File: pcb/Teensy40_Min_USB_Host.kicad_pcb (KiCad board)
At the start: 2 copper layers, 17.8 x 45.7 mm, 17 parts, among them J1 USB_A, J2 Conn_01x14, J3 Conn_01x14, U1 TPD3S014, U2 Teensy4.0

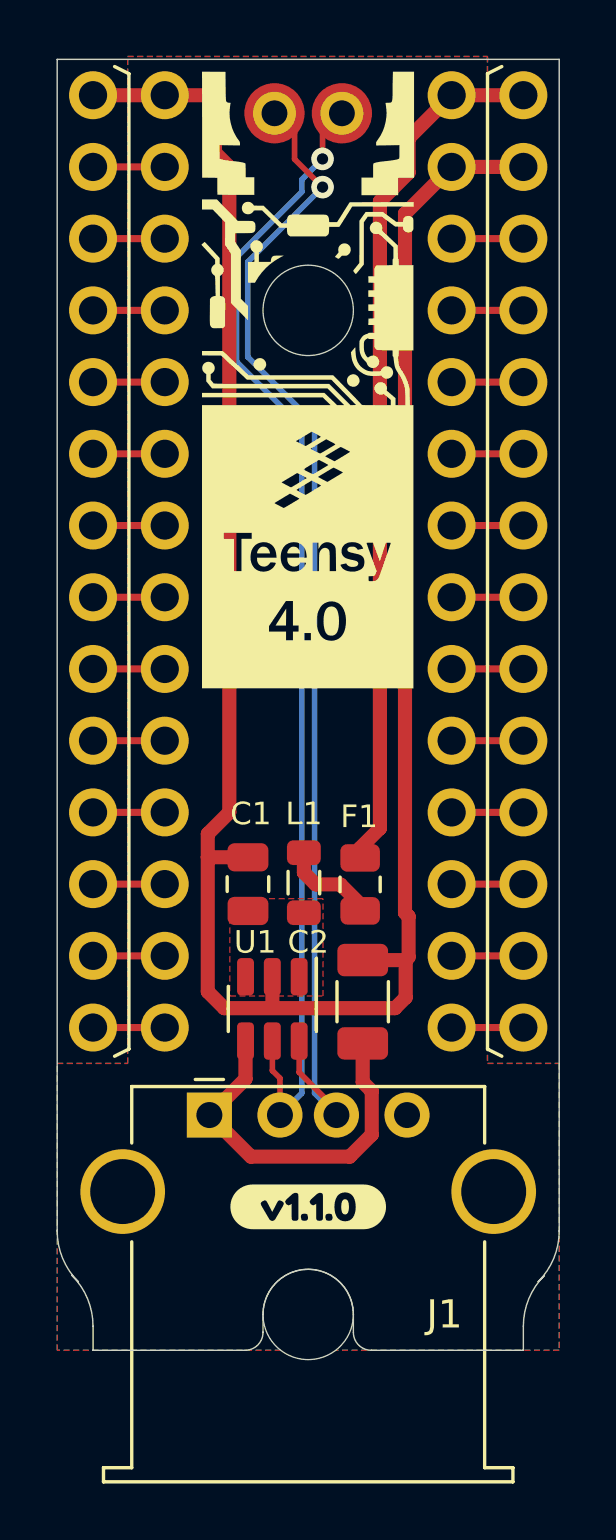
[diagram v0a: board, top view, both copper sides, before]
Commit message: Update version footprint to 1.2.0
This is also now positioned underneath the Teensy instead of underneath the USB port, for visibility whenever the circuit is fully soldered.
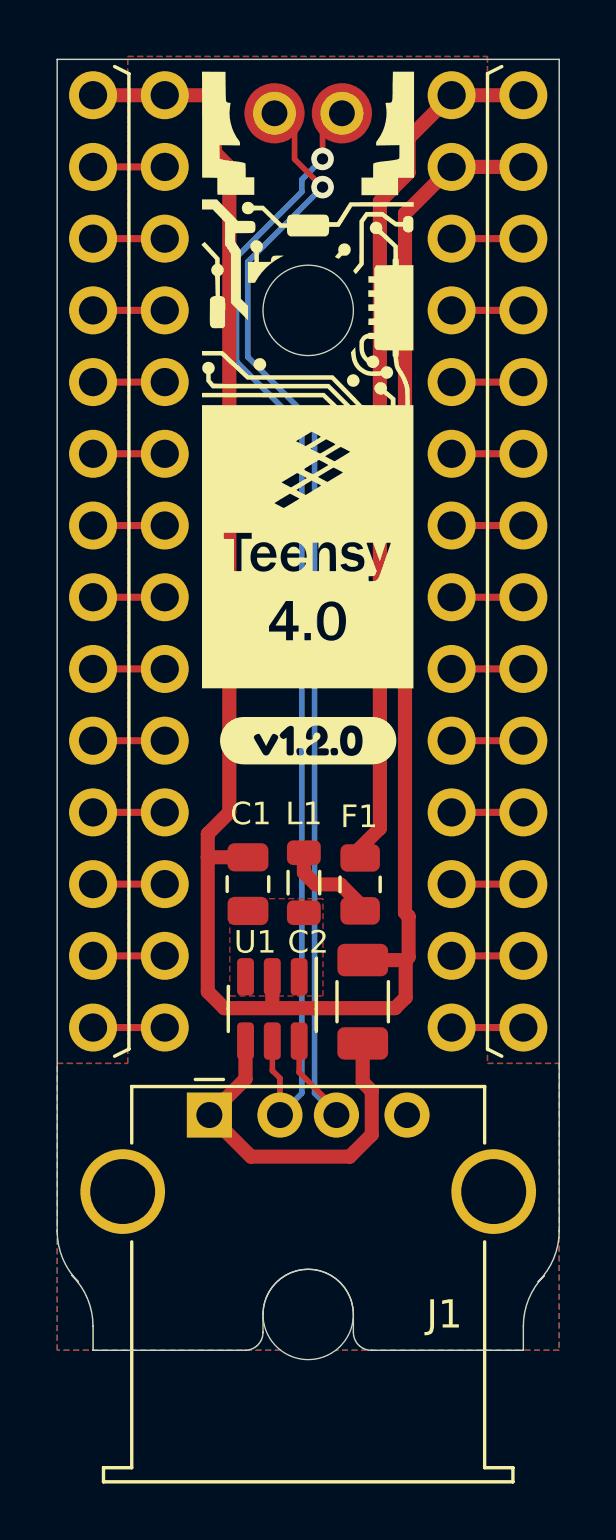
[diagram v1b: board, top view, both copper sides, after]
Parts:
- removed kibuzzard-621DE22F: G***, kibuzzard-621DE22F
- added kibuzzard-628AF6F2: G***, kibuzzard-628AF6F2, F.Cu at (149.9, 105.4)

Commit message: Replace C2 cap with tantalum, 150 uF
Having some suspected brownout issues with rumble motors using the 100 uF ceramic cap, and I found some documentation from TI that says the USB host output capacitance should be 120 µF at a minimum.
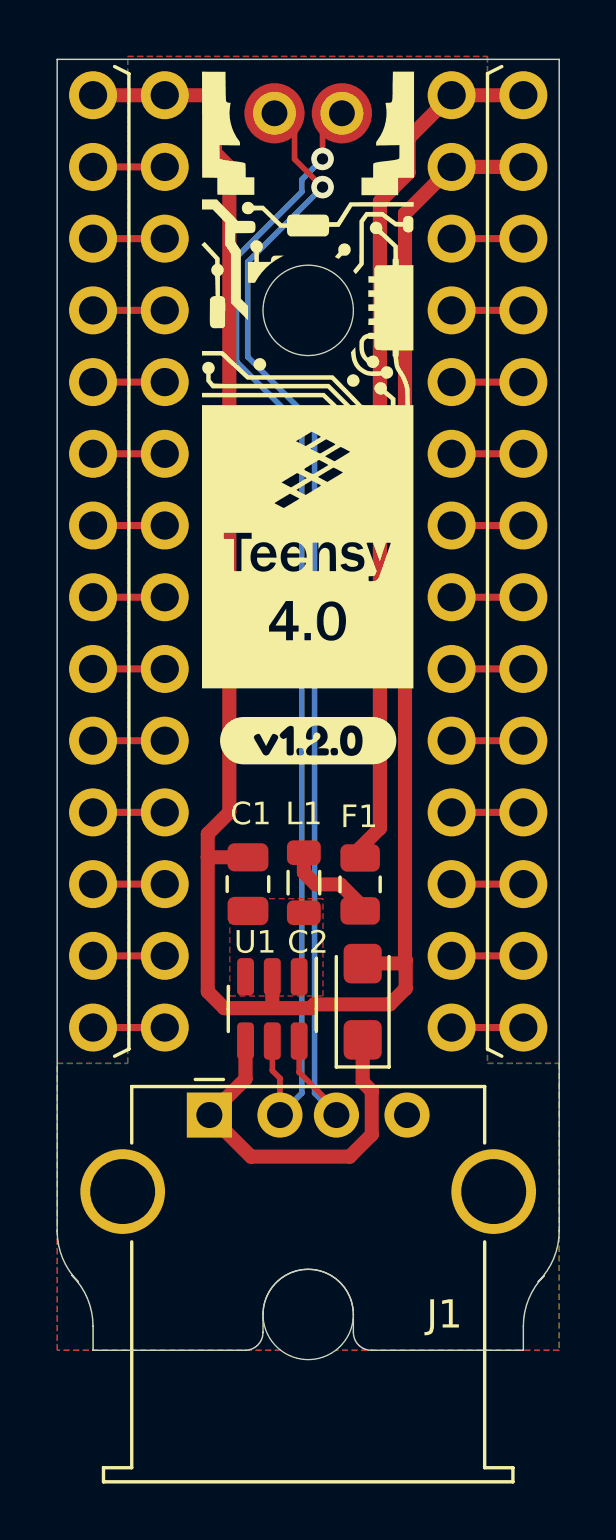
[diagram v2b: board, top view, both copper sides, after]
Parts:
- C2: value 100 µF -> 150 µF; footprint Capacitor_SMD:C_1206_3216Metric -> Capacitor_Tantalum_SMD:CP_EIA-3216-10_Kemet-I
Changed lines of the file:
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@@
       (net 1 "VCC") (pinfunction "VIN") (pintype "power_in"))
   )
+  (footprint "Capacitor_Tantalum_SMD:CP_EIA-3216-10_Kemet-I" (layer "F.Cu")
+    (at 151.7904 114.6556 90)
+    (descr "Tantalum Capacitor SMD Kemet-I (3216-10 Metric), IPC_7351 nominal, (Body size from: http://www.kemet.com/Lists/ProductCatalog/Attachments/253/KEM_TC101_STD.pdf), generated with kicad-footprint-generator")
+    (tags "capacitor tantalum")
+    (property "Description" "CAP TANT 150UF 20% 6.3V 1206")
+    (property "DigiKey Product Number" "478-6250-1-ND")
+    (property "Manufacturer" "KYOCERA AVX")
+    (property "Manufacturer Product Number" "TLNK157M006R2500")
+    (property "Sheetfile" "Teensy40_Min_USB_Host.kicad_sch")
+    (property "Sheetname" "")
+    (attr smd)
+    (fp_text reference "C2" (at 2.1056 -1.9404 180) (layer "F.SilkS")
+      (effects (font (size 0.8 0.8) (thickness 0.15)))
+    )
+    (fp_text value "150 µF" (at 0 1.75 90) (layer "F.Fab")
+      (effects (font (size 1 1) (thickness 0.15)))
+    )
+    (fp_text user "${REFERENCE}" (at 0 0 180) (layer "F.Fab")
+      (effects (font (size 0.8 0.8) (thickness 0.12)))
+    )
+    (fp_line (start 1.6 -0.935) (end -2.31 -0.935) (layer "F.SilkS") (width 0.12))
+    (fp_line (start -2.31 -0.935) (end -2.31 0.935) (layer "F.SilkS") (width 0.12))
+    (fp_line (start -2.31 0.935) (end 1.6 0.935) (layer "F.SilkS") (width 0.12))
+    (fp_line (start 2.3 -1.05) (end 2.3 1.05) (layer "F.CrtYd") (width 0.05))
+    (fp_line (start -2.3 1.05) (end -2.3 -1.05) (layer "F.CrtYd") (width 0.05))
+    (fp_line (start -2.3 -1.05) (end 2.3 -1.05) (layer "F.CrtYd") (width 0.05))
+    (fp_line (start 2.3 1.05) (end -2.3 1.05) (layer "F.CrtYd") (width 0.05))
+    (fp_line (start 1.6 -0.8) (end -1.2 -0.8) (layer "F.Fab") (width 0.1))
+    (fp_line (start -1.6 0.8) (end 1.6 0.8) (layer "F.Fab") (width 0.1))
+    (fp_line (start -1.2 -0.8) (end -1.6 -0.4) (layer "F.Fab") (width 0.1))
+    (fp_line (start -1.6 -0.4) (end -1.6 0.8) (layer "F.Fab") (width 0.1))
+    (fp_line (start 1.6 0.8) (end 1.6 -0.8) (layer "F.Fab") (width 0.1))
+    (pad "1" smd roundrect (at -1.35 0 90) (size 1.4 1.35) (layers "F.Cu" "F.Paste" "F.Mask") (roundrect_rratio 0.185185)
+      (net 3 "/VBUS") (pintype "passive"))
+    (pad "2" smd roundrect (at 1.35 0 90) (size 1.4 1.35) (layers "F.Cu" "F.Paste" "F.Mask") (roundrect_rratio 0.185185)
+      (net 2 "GND") (pintype "passive"))
+    (model "${KICAD6_3DMODEL_DIR}/Capacitor_Tantalum_SMD.3dshapes/CP_EIA-3216-10_Kemet-I.wrl"
+      (offset (xyz 0 0 0))
+      (scale (xyz 1 1 1))
+      (rotate (xyz 0 0 0))
+    )
+  )
   (footprint "Inductor_SMD:L_0805_2012Metric" (layer "F.Cu")
     (at 149.7076 110.4392 -90)
@@
     )
   )
-  (footprint "Capacitor_SMD:C_1206_3216Metric" (layer "F.Cu")
-    (at 151.7904 114.6556 90)
-    (descr "Capacitor SMD 1206 (3216 Metric), square (rectangular) end terminal, IPC_7351 nominal, (Body size source: IPC-SM-782 page 76, https://www.pcb-3d.com/wordpress/wp-content/uploads/ipc-sm-782a_amendment_1_and_2.pdf), generated with kicad-footprint-generator")
-    (tags "capacitor")
-    (property "Description" "CAP CER 100UF 6.3V X5R 1206")
-    (property "DigiKey Product Number" "13-CC1206MKX5R5BB107CT-ND")
-    (property "Manufacturer" "YAGEO")
-    (property "Manufacturer Product Number" "CC1206MKX5R5BB107")
-    (property "Sheetfile" "Teensy40_Min_USB_Host.kicad_sch")
-    (property "Sheetname" "")
-    (attr smd)
-    (fp_text reference "C2" (at 2.1082 -1.9304) (layer "F.SilkS")
-      (effects (font (size 0.8 0.8) (thickness 0.15)))
-    )
-    (fp_text value "100 µF" (at 0 1.85 90) (layer "F.Fab")
-      (effects (font (size 1 1) (thickness 0.15)))
-    )
-    (fp_text user "${REFERENCE}" (at 0 0 180) (layer "F.Fab")
-      (effects (font (size 0.8 0.8) (thickness 0.12)))
-    )
-    (fp_line (start -0.711252 0.91) (end 0.711252 0.91) (layer "F.SilkS") (width 0.12))
-    (fp_line (start -0.711252 -0.91) (end 0.711252 -0.91) (layer "F.SilkS") (width 0.12))
-    (fp_line (start 2.3 1.15) (end -2.3 1.15) (layer "F.CrtYd") (width 0.05))
-    (fp_line (start 2.3 -1.15) (end 2.3 1.15) (layer "F.CrtYd") (width 0.05))
-    (fp_line (start -2.3 1.15) (end -2.3 -1.15) (layer "F.CrtYd") (width 0.05))
-    (fp_line (start -2.3 -1.15) (end 2.3 -1.15) (layer "F.CrtYd") (width 0.05))
-    (fp_line (start -1.6 0.8) (end -1.6 -0.8) (layer "F.Fab") (width 0.1))
-    (fp_line (start 1.6 0.8) (end -1.6 0.8) (layer "F.Fab") (width 0.1))
-    (fp_line (start -1.6 -0.8) (end 1.6 -0.8) (layer "F.Fab") (width 0.1))
-    (fp_line (start 1.6 -0.8) (end 1.6 0.8) (layer "F.Fab") (width 0.1))
-    (pad "1" smd roundrect locked (at -1.475 0 90) (size 1.15 1.8) (layers "F.Cu" "F.Paste" "F.Mask") (roundrect_rratio 0.2173913043)
-      (net 3 "/VBUS") (pintype "passive"))
-    (pad "2" smd roundrect locked (at 1.475 0 90) (size 1.15 1.8) (layers "F.Cu" "F.Paste" "F.Mask") (roundrect_rratio 0.2173913043)
-      (net 2 "GND") (pintype "passive"))
-    (model "${KICAD6_3DMODEL_DIR}/Capacitor_SMD.3dshapes/C_1206_3216Metric.wrl"
-      (offset (xyz 0 0 0))
-      (scale (xyz 1 1 1))
-      (rotate (xyz 0 0 0))
-    )
-  )
   (footprint "Fuse:Fuse_0805_2012Metric" (layer "F.Cu")
     (at 151.7 110.5 -90)
@@
   (segment (start 151.7 109.2131) (end 152.4 108.5131) (width 0.5) (layer "F.Cu") (net 1))
   (segment (start 147.066 107.95) (end 147.066 85.09) (width 0.5) (layer "F.Cu") (net 2))
-  (segment (start 146.88812 114.88412) (end 152.93348 114.88412) (width 0.5) (layer "F.Cu") (net 2))
   (segment (start 146.558 84.582) (end 146.558 82.55) (width 0.5) (layer "F.Cu") (net 2))
-  (segment (start 153.416 113.0772) (end 153.3126 113.1806) (width 0.5) (layer "F.Cu") (net 2))
+  (segment (start 149.938329 114.88412) (end 150.072449 114.75) (width 0.5) (layer "F.Cu") (net 2))
+  (segment (start 151.9098 113.3) (end 153.1932 113.3) (width 0.5) (layer "F.Cu") (net 2))
+  (segment (start 152.75 114.75) (end 153.3126 114.1874) (width 0.5) (layer "F.Cu") (net 2))
+  (segment (start 150.072449 114.75) (end 152.75 114.75) (width 0.5) (layer "F.Cu") (net 2))
+  (segment (start 154.94 85.09) (end 153.289 86.741) (width 0.5) (layer "F.Cu") (net 2))
   (segment (start 146.304 109.54) (end 146.304 108.712) (width 0.5) (layer "F.Cu") (net 2))
   (segment (start 142.24 82.55) (end 144.78 82.55) (width 0.5) (layer "F.Cu") (net 2))
@@
   (segment (start 146.304 108.712) (end 147.066 107.95) (width 0.5) (layer "F.Cu") (net 2))
   (segment (start 147.066 85.09) (end 146.558 84.582) (width 0.5) (layer "F.Cu") (net 2))
-  (segment (start 153.416 111.633) (end 153.416 113.0772) (width 0.5) (layer "F.Cu") (net 2))
-  (segment (start 152.93348 114.88412) (end 153.3126 114.505) (width 0.5) (layer "F.Cu") (net 2))
+  (segment (start 153.3126 114.1874) (end 153.3126 113.1806) (width 0.5) (layer "F.Cu") (net 2))
+  (segment (start 146.304 109.54) (end 146.304 114.3) (width 0.5) (layer "F.Cu") (net 2))
+  (segment (start 153.289 113.157) (end 153.3126 113.1806) (width 0.5) (layer "F.Cu") (net 2))
+  (segment (start 153.1932 113.3) (end 153.3126 113.1806) (width 0.5) (layer "F.Cu") (net 2))
+  (segment (start 153.289 86.741) (end 153.289 113.157) (width 0.5) (layer "F.Cu") (net 2))
   (segment (start 148.59 113.7721) (end 148.59 114.8588) (width 0.5) (layer "F.Cu") (net 2))
-  (segment (start 153.3126 114.505) (end 153.3126 113.1806) (width 0.5) (layer "F.Cu") (net 2))
-  (segment (start 153.416 111.633) (end 153.289 111.506) (width 0.5) (layer "F.Cu") (net 2))
-  (segment (start 146.88812 114.88412) (end 146.304 114.3) (width 0.5) (layer "F.Cu") (net 2))
-  (segment (start 153.289 111.506) (end 153.289 86.741) (width 0.5) (layer "F.Cu") (net 2))
-  (segment (start 146.304 114.3) (end 146.304 109.54) (width 0.5) (layer "F.Cu") (net 2))
-  (segment (start 151.7904 113.1806) (end 153.3126 113.1806) (width 0.5) (layer "F.Cu") (net 2))
-  (segment (start 153.289 86.741) (end 154.94 85.09) (width 0.5) (layer "F.Cu") (net 2))
+  (segment (start 146.88812 114.88412) (end 149.938329 114.88412) (width 0.5) (layer "F.Cu") (net 2))
+  (segment (start 146.304 114.3) (end 146.88812 114.88412) (width 0.5) (layer "F.Cu") (net 2))
   (segment (start 152.109511 119.365689) (end 152.109511 117.819511) (width 0.5) (layer "F.Cu") (net 3))
   (segment (start 151.3332 120.142) (end 147.8332 120.142) (width 0.5) (layer "F.Cu") (net 3))

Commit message: Add VBUS label to schematic
Better than using a local label standalone.
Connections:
- net /VBUS renamed VBUS
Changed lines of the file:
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@@
   (net 1 "VCC")
   (net 2 "GND")
-  (net 3 "/VBUS")
+  (net 3 "VBUS")
   (net 4 "/D-")
   (net 5 "/D+")
@@
     (fp_line (start 1.6 0.8) (end 1.6 -0.8) (layer "F.Fab") (width 0.1))
     (pad "1" smd roundrect (at -1.35 0 90) (size 1.4 1.35) (layers "F.Cu" "F.Paste" "F.Mask") (roundrect_rratio 0.185185)
-      (net 3 "/VBUS") (pintype "passive"))
+      (net 3 "VBUS") (pintype "passive"))
     (pad "2" smd roundrect (at 1.35 0 90) (size 1.4 1.35) (layers "F.Cu" "F.Paste" "F.Mask") (roundrect_rratio 0.185185)
       (net 2 "GND") (pintype "passive"))
@@
       (net 32 "/VIN") (pinfunction "IN") (pintype "power_in"))
     (pad "4" smd roundrect locked (at 1.1375 0.95 270) (size 1.325 0.6) (layers "F.Cu" "F.Paste" "F.Mask") (roundrect_rratio 0.25)
-      (net 3 "/VBUS") (pinfunction "OUT") (pintype "passive"))
+      (net 3 "VBUS") (pinfunction "OUT") (pintype "passive"))
     (pad "5" smd roundrect locked (at 1.1375 0 270) (size 1.325 0.6) (layers "F.Cu" "F.Paste" "F.Mask") (roundrect_rratio 0.25)
       (net 4 "/D-") (pinfunction "D1") (pintype "passive"))
@@
     (fp_line (start -2.75 -1.01) (end 9.75 -1.01) (layer "F.Fab") (width 0.1))
     (pad "1" thru_hole rect locked (at 0 0) (size 1.6 1.6) (drill 0.92) (layers *.Cu *.Mask)
-      (net 3 "/VBUS") (pinfunction "VBUS") (pintype "power_in"))
+      (net 3 "VBUS") (pinfunction "VBUS") (pintype "power_in"))
     (pad "2" thru_hole circle locked (at 2.5 0) (size 1.6 1.6) (drill 0.92) (layers *.Cu *.Mask)
       (net 4 "/D-") (pinfunction "D-") (pintype "bidirectional"))

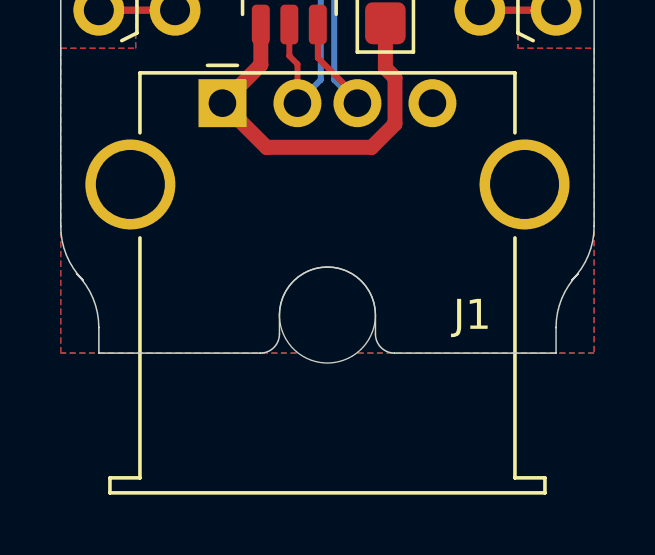
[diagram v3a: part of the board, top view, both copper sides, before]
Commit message: Remove H2 mounting hole
This semi-circle is now part of the board outline, and the radius (1.6 mm) is large enough for most board houses that a separate drill is not needed.
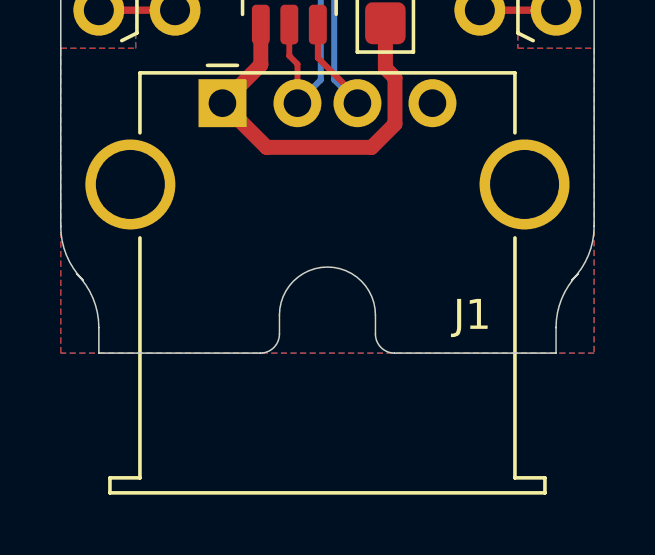
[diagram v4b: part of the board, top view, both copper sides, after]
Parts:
- removed H2: MountingHole, Teensy40_Min_USB_Host:MountingHole_3.2mm
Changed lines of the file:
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@@
       ) (layer "F.SilkS") (width 0) (fill solid))
-  )
-  (footprint "Teensy40_Min_USB_Host:MountingHole_3.2mm" (layer "F.Cu")
-    (at 149.86 125.73)
-    (descr "Mounting Hole 3.2mm, no annular, M3")
-    (tags "mounting hole 3.2mm no annular m3")
-    (property "Description" "~")
-    (property "DigiKey Product Number" "~")
-    (property "Manufacturer" "~")
-    (property "Manufacturer Product Number" "~")
-    (property "Sheetfile" "Teensy40_Min_USB_Host.kicad_sch")
-    (property "Sheetname" "")
-    (property "exclude_from_bom" "")
-    (attr exclude_from_pos_files exclude_from_bom)
-    (fp_text reference "H2" (at 0 -2.54) (layer "F.SilkS") hide
-      (effects (font (size 1 1) (thickness 0.15)))
-    )
-    (fp_text value "MountingHole" (at 0 2.54) (layer "F.Fab") hide
-      (effects (font (size 1 1) (thickness 0.15)))
-    )
-    (fp_text user "${REFERENCE}" (at 0.3 0) (layer "F.Fab") hide
-      (effects (font (size 1 1) (thickness 0.15)))
-    )
-    (pad "" np_thru_hole circle (at 0 0) (size 3.2 3.2) (drill 3.2) (layers *.Cu *.Mask))
   )
   (footprint "Package_TO_SOT_SMD:SOT-23-6" (layer "F.Cu")
@@
       ) (layer "B.SilkS") (width 0) (fill solid))
   )
+  (gr_circle locked (center 149.86 125.73) (end 151.46 125.73) (layer "Dwgs.User") (width 0.05) (fill none))
   (gr_arc (start 148.26 126.365) (mid 148.074013 126.814013) (end 147.625 127) (layer "Edge.Cuts") (width 0.05))
   (gr_line (start 158.006051 124.568949) (end 158.223949 124.351051) (layer "Edge.Cuts") (width 0.05))
